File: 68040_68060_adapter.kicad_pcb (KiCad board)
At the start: 2 copper layers, 59.1 x 95.6 mm, 30 parts, among them IC2 74F257, IC3 MC68060RCPGA_BIG, IC4 LMS1585-3.3, U4$1 4POL, U6$1 6POL

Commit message: Updated C values
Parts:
- C1, C4: value 10u -> 100n
- C5, C6: value 100n -> 10u

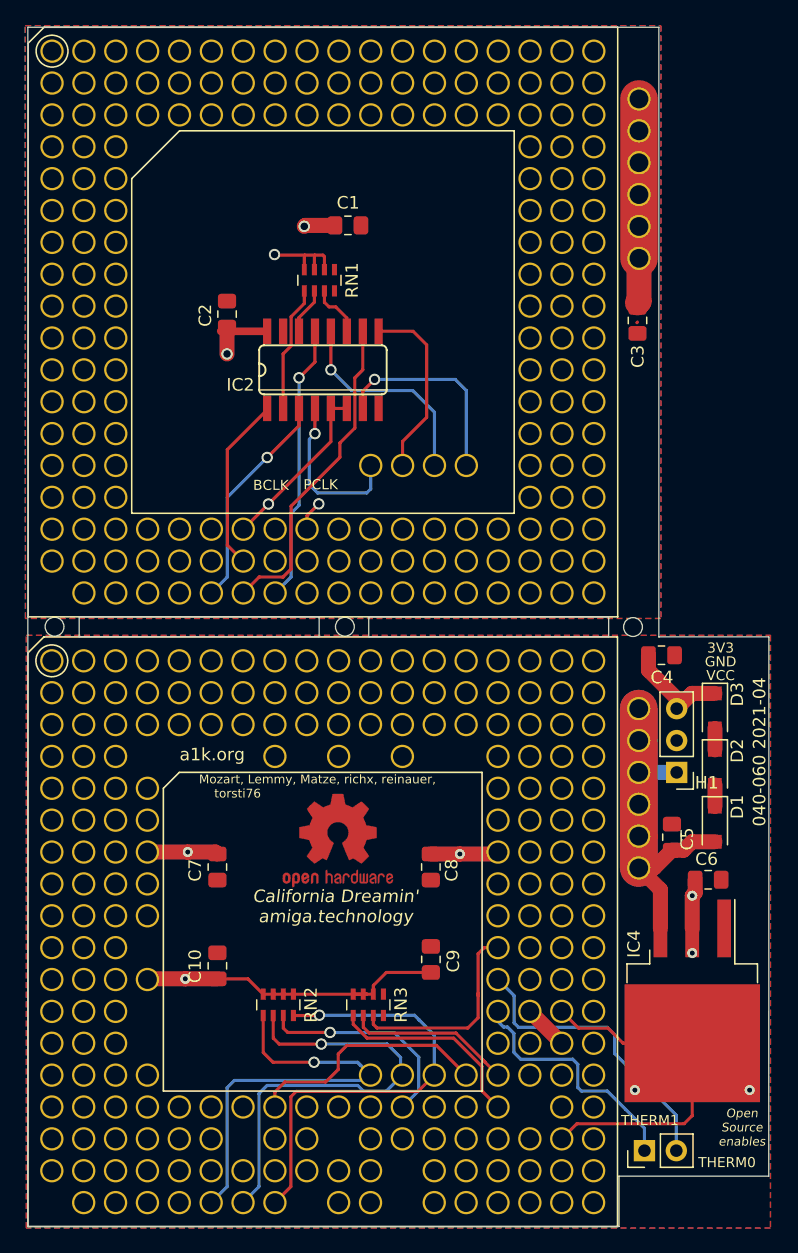
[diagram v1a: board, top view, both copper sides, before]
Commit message: Redesign with better clearance, unified Via sizes, better routing...
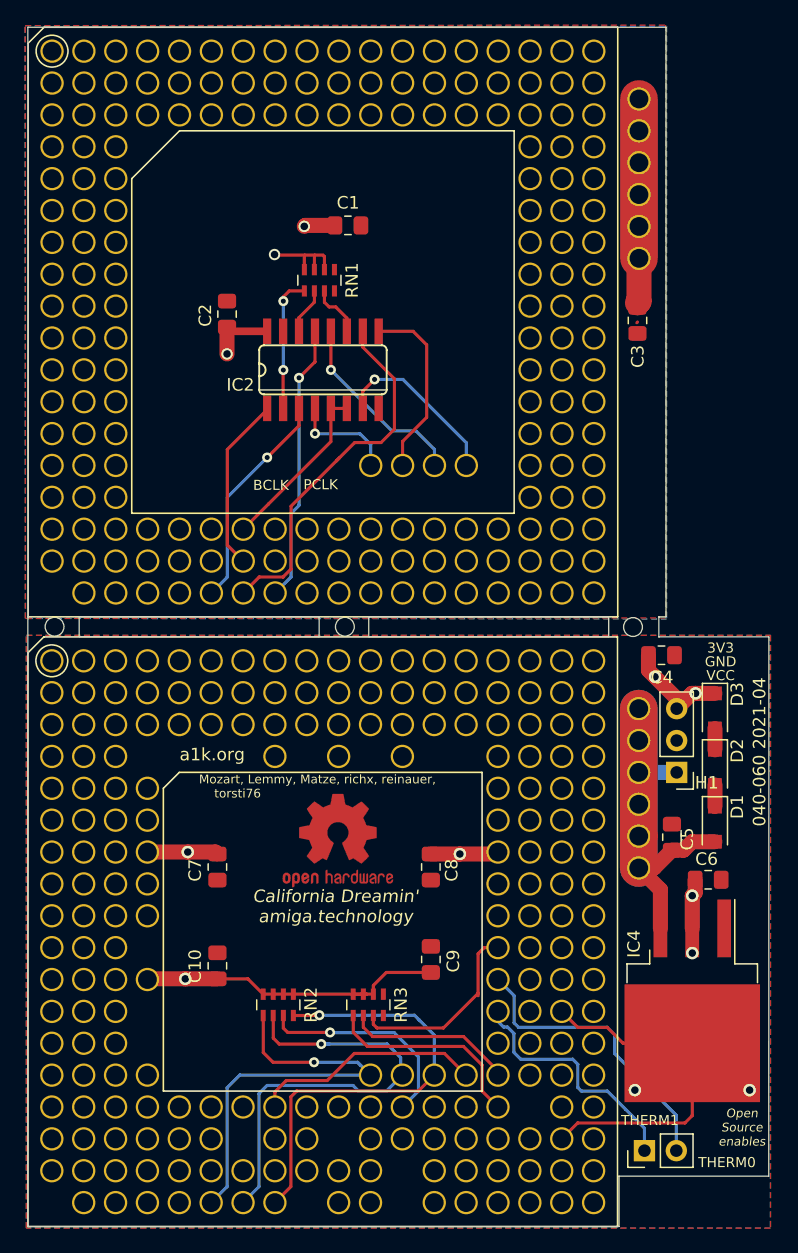
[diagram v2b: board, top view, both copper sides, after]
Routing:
- net 60_IPL2: track 13.4 -> 8.48 mm
- net 40_IPL1: track 25.9 -> 29.6 mm
- net GND: track 4.53 -> 0.94 mm
- net 60_CLKEN: track 16.4 -> 13.9 mm
- net 40_PCLK: track 2.41 -> 0.00 mm, vias 1 -> 0
- net 60_IPL0: track 17.0 -> 15.3 mm
- net CLKEN: track 19.7 -> 18.4 mm
- net CLA: track 16.6 -> 15.5 mm
- net VCC: track 31.3 -> 30.2 mm
- net N$1: track 10.1 -> 10.8 mm, vias 0 -> 2
- net IPL1: track 35.2 -> 35.8 mm
- net 40_BCLK: vias 1 -> 0
- net +3V3: vias 7 -> 9
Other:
- outline, holes or cut-outs redrawn
- net class Default: clearance 0.1524 -> 0.2
- rule trace_clearance: 0.1524 -> 0.2

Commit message: Cosmetics
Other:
- board text removed: "BCLK"
- board text removed: "PCLK"
